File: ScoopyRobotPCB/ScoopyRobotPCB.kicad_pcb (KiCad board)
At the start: 2 copper layers, 25 parts, among them J1 18V battery, J2 Raspberry_Pi_Header, J3 Power, J4 Wheels, J5 Power, J6 Loading, J7 Left, J8 Right, M3 Left motor, M4 Right motor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

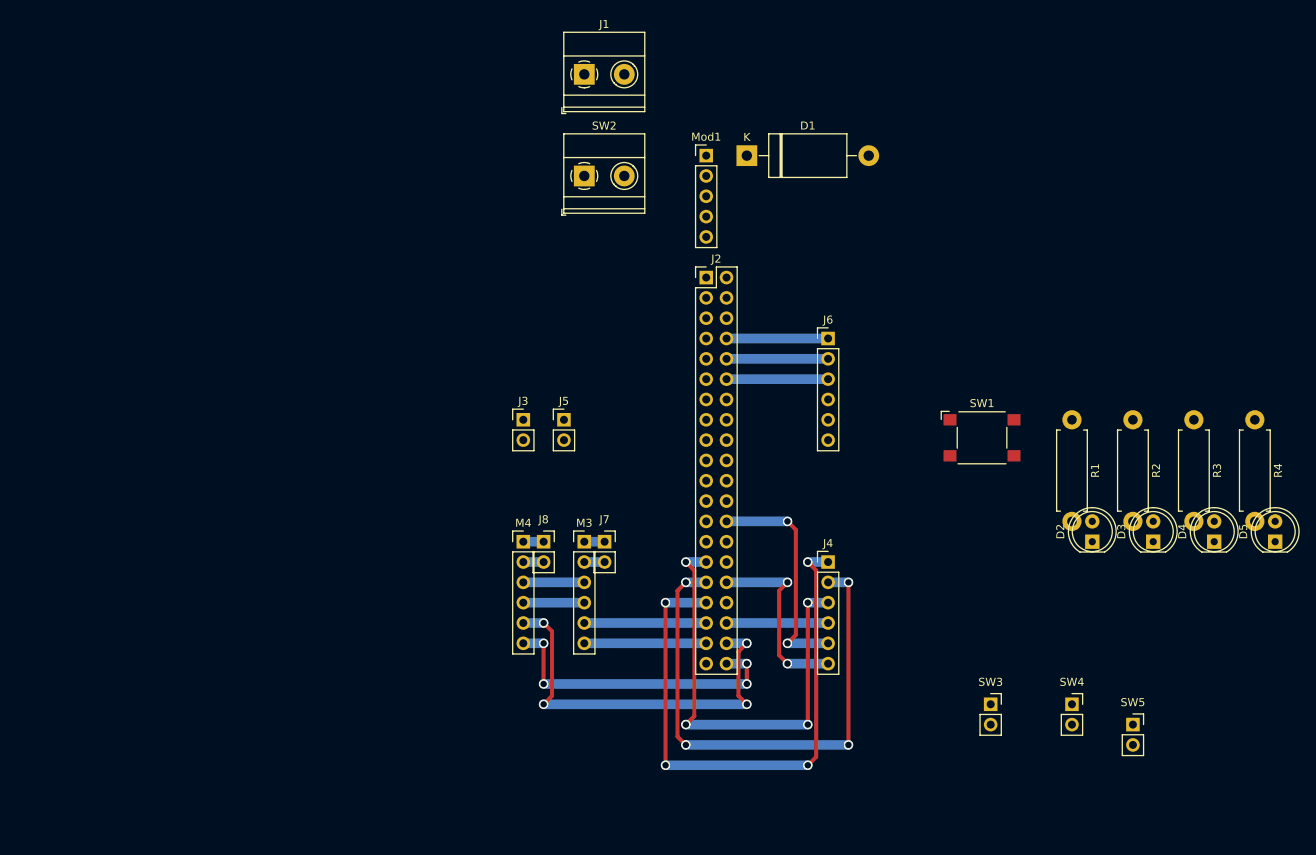
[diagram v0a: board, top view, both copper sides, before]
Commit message: Added voltage dividers for encoder, need to update layout to make way for ethernet header
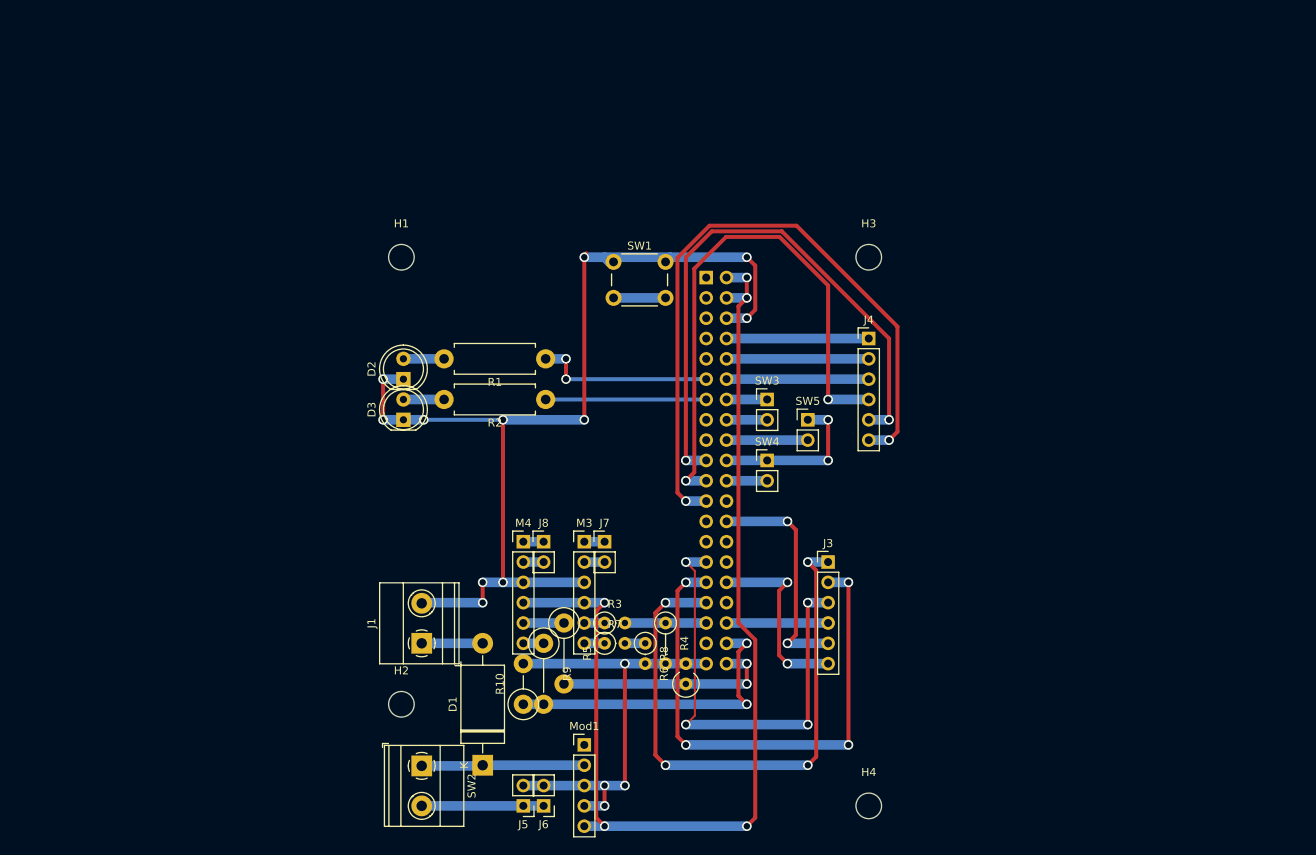
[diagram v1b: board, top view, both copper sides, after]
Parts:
- removed D4, D5: LED, LED_THT:LED_D5.0mm
- added H1: MountingHole, MountingHole:MountingHole_3.2mm_M3, F.Cu at (88.9, 76.2)
- added H2: MountingHole, MountingHole:MountingHole_3.2mm_M3, F.Cu at (88.9, 132.1)
- added H3: MountingHole, MountingHole:MountingHole_3.2mm_M3, F.Cu at (147.3, 76.2)
- added H4: MountingHole, MountingHole:MountingHole_3.2mm_M3, F.Cu at (147.3, 144.8)
- added R10: 2.2k, Resistor_THT:R_Axial_DIN0411_L9.9mm_D3.6mm_P5.08mm_Vertical, F.Cu at (104.1, 132.1)
- added R5: 1.5k, Resistor_THT:R_Axial_DIN0411_L9.9mm_D3.6mm_P7.62mm_Vertical, F.Cu at (109.2, 121.9)
- added R6: 2.2k, Resistor_THT:R_Axial_DIN0309_L9.0mm_D3.2mm_P2.54mm_Vertical, F.Cu at (124.5, 129.5)
- added R7: 1.5k, Resistor_THT:R_Axial_DIN0207_L6.3mm_D2.5mm_P2.54mm_Vertical, F.Cu at (114.3, 124.5)
- added R8: 2.2k, Resistor_THT:R_Axial_DIN0207_L6.3mm_D2.5mm_P2.54mm_Vertical, F.Cu at (119.4, 124.5)
- added R9: 1.5k, Resistor_THT:R_Axial_DIN0411_L9.9mm_D3.6mm_P7.62mm_Vertical, F.Cu at (106.7, 124.5)
- J2: footprint Connector_PinHeader_2.54mm:PinHeader_2x20_P2.54mm_Vertical -> Connector_PinSocket_2.54mm:PinSocket_2x20_P2.54mm_Vertical; moved to B.Cu
- J7, J8, SW3, SW4, SW5: footprint Connector_PinSocket_2.54mm:PinSocket_1x02_P2.54mm_Vertical -> Connector_PinHeader_2.54mm:PinHeader_1x02_P2.54mm_Vertical
- R3: value 220 -> 1.5k; footprint Resistor_THT:R_Axial_DIN0411_L9.9mm_D3.6mm_P12.70mm_Horizontal -> Resistor_THT:R_Axial_DIN0207_L6.3mm_D2.5mm_P2.54mm_Vertical
- R4: value 220 -> 2.2k; footprint Resistor_THT:R_Axial_DIN0411_L9.9mm_D3.6mm_P12.70mm_Horizontal -> Resistor_THT:R_Axial_DIN0207_L6.3mm_D2.5mm_P5.08mm_Vertical
- SW1: footprint Button_Switch_SMD:SW_SPST_Omron_B3FS-100xP -> Button_Switch_THT:SW_PUSH_6mm
- moved D3 95.0 mm to (89.2, 96.5)
- moved D2 88.5 mm to (89.2, 91.4)
- moved D1 83.0 mm to (99.1, 139.7), turned to 90 degrees
- moved R3 77.9 mm to (114.3, 121.9), turned to 0 degrees
- moved R4 77.9 mm to (121.9, 121.9)
- moved SW2 76.5 mm to (91.4, 139.8), turned to -90 degrees
- moved Mod1 75.2 mm to (111.8, 137.2)
- moved J1 74.0 mm to (91.4, 124.5), turned to 90 degrees
- moved R2 73.4 mm to (106.9, 94.0), turned to 180 degrees
- moved R1 66.2 mm to (106.9, 88.9), turned to 180 degrees
- moved SW5 55.7 mm to (139.7, 96.5)
- moved SW1 51.0 mm to (115.4, 76.8)
- moved SW4 48.8 mm to (134.6, 101.6)
- moved J6 48.3 mm to (106.7, 144.8), turned to 180 degrees
- moved J5 48.3 mm to (104.1, 144.8), turned to 180 degrees
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- renumbered J4 to J3, J6 to J4, J3 to J5, J5 to J6
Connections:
- J2 pad 11: /UI.LED2 -> /UI.LED0
- J2 pad 13: /UI.LED3 -> /UI.LED1
- J2 pad 3: /UI.SW -> unconnected-(J2-GPIO02/SDA-Pad3)
- J2 pad 5: /UI.LED0 -> unconnected-(J2-GPIO03/SCL-Pad5)
- J2 pad 7: /UI.LED1 -> /UI.SW
- M3 pad 5: /L.Enc_A -> Net-(M3-Enc_A)
- M3 pad 6: /L.Enc_B -> Net-(M3-Enc_B)
- M4 pad 5: /R.Enc_A -> Net-(M4-Enc_A)
- M4 pad 6: /R.Enc_B -> Net-(M4-Enc_B)
- R3 pad 1: /UI.LED2 -> Net-(M3-Enc_A)
- R3 pad 2: Net-(D4-A) -> /L.Enc_A
- R4 pad 1: /UI.LED3 -> /L.Enc_A
- R4 pad 2: Net-(D5-A) -> GND
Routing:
- net GND: track 7.62 -> 212.0 mm, vias 0 -> 17
- net +5V: track 7.62 -> 134.7 mm, vias 0 -> 5
- net /Tray.En: track 0.00 -> 84.9 mm, vias 0 -> 2
- net /Tray.Mot_A: track 0.00 -> 72.9 mm, vias 0 -> 2
- net /Tray.Mot_B: track 0.00 -> 69.7 mm, vias 0 -> 2
- net /UI.LED0: track 0.00 -> 22.6 mm, vias 0 -> 2
- net +BATT: track 0.00 -> 20.4 mm
- net /UI.LED1: track 0.00 -> 20.1 mm
- net Vdrive: track 0.00 -> 15.2 mm
- net /L.Enc_B: track 15.2 -> 2.54 mm
- net /R.Enc_A: track 50.0 -> 39.0 mm, vias 4 -> 2
- net /Tray up: track 0.00 -> 10.2 mm
- net /R.Enc_B: track 38.1 -> 27.9 mm, vias 4 -> 2
- net Net-(D1-A): track 0.00 -> 7.62 mm
- net /UI.SW: track 0.00 -> 6.50 mm
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
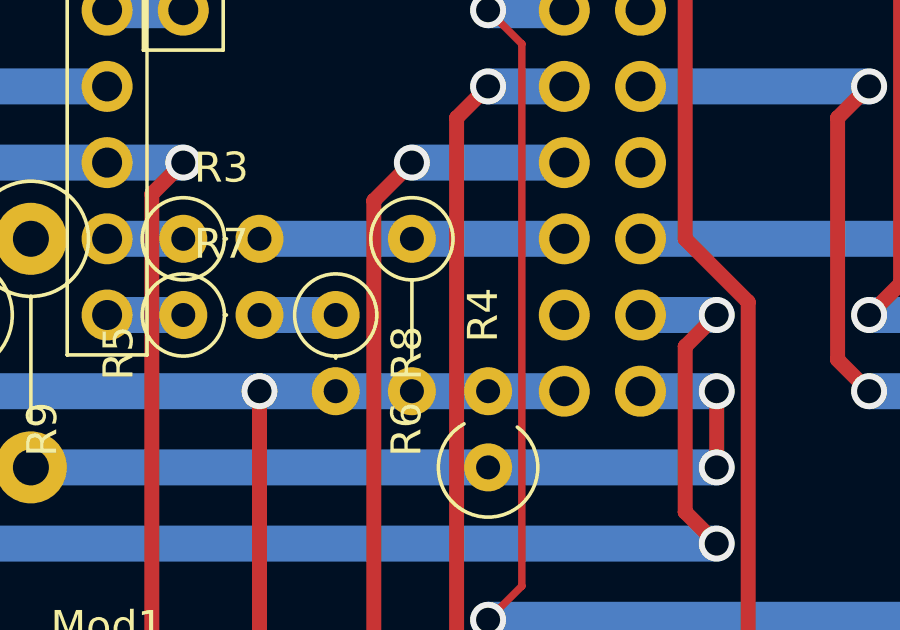
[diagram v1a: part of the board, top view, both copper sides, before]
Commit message: Added missing track on PCB
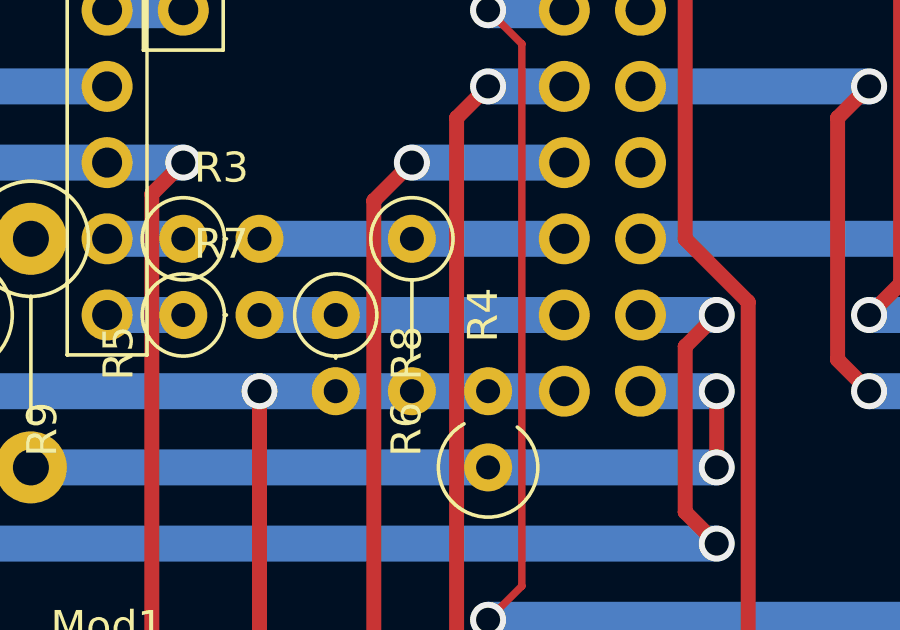
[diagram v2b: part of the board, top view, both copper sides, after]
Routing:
- net /L.Enc_B: track 2.54 -> 10.2 mm
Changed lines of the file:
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@@
+	)
+	(segment
+		(start 119.38 124.46)
+		(end 127 124.46)
+		(width 1.2)
+		(layer "B.Cu")
+		(net 17)
 	)
 	(segment

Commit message: Schematic finished
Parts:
- removed the J6 at (106.7, 144.8)
- removed SW4: Tray down, Connector_PinHeader_2.54mm:PinHeader_1x02_P2.54mm_Vertical
- removed SW5: Tray up, Connector_PinHeader_2.54mm:PinHeader_1x02_P2.54mm_Vertical
- added D4: 1N4004, Diode_THT:D_DO-41_SOD81_P10.16mm_Horizontal, F.Cu at (144.8, 86.4)
- added J3: Left colour sensor, Connector_PinHeader_2.54mm:PinHeader_1x04_P2.54mm_Vertical, F.Cu at (121.9, 86.4)
- added Q1: Q_NPN_Darlington_BCE, Package_TO_SOT_THT:TO-220-3_Vertical, F.Cu at (114.3, 59.4)
- added R3: 390, Resistor_THT:R_Axial_DIN0411_L9.9mm_D3.6mm_P7.62mm_Vertical, F.Cu at (113.6, 52.9)
- J4: value Loading -> Right colour sensor; footprint Connector_PinHeader_2.54mm:PinHeader_1x06_P2.54mm_Vertical -> Connector_PinHeader_2.54mm:PinHeader_1x04_P2.54mm_Vertical
- R10: renamed from R9; value 1.5k -> 10k
- R11: renamed from R10; value 2.2k -> 10k
- R4: renamed from R3; value 1.5k -> 10k; footprint Resistor_THT:R_Axial_DIN0207_L6.3mm_D2.5mm_P2.54mm_Vertical -> Resistor_THT:R_Axial_DIN0411_L9.9mm_D3.6mm_P7.62mm_Vertical
- R5: renamed from R4; value 2.2k -> 10k; footprint Resistor_THT:R_Axial_DIN0207_L6.3mm_D2.5mm_P5.08mm_Vertical -> Resistor_THT:R_Axial_DIN0207_L6.3mm_D2.5mm_P2.54mm_Vertical
- R6: renamed from R5; value 1.5k -> 10k
- R7: renamed from R6; value 2.2k -> 10k
- R8: renamed from R7; value 1.5k -> 10k; footprint Resistor_THT:R_Axial_DIN0207_L6.3mm_D2.5mm_P2.54mm_Vertical -> Resistor_THT:R_Axial_DIN0411_L9.9mm_D3.6mm_P7.62mm_Vertical
- R9: renamed from R8; value 2.2k -> 10k; footprint Resistor_THT:R_Axial_DIN0207_L6.3mm_D2.5mm_P2.54mm_Vertical -> Resistor_THT:R_Axial_DIN0411_L9.9mm_D3.6mm_P5.08mm_Vertical
- moved H1 43.4 mm to (45.5, 76.2)
- moved D2 43.4 mm to (45.7, 91.4)
- moved D3 43.4 mm to (45.7, 96.5)
- moved R1 43.4 mm to (63.5, 88.9)
- moved R2 43.4 mm to (63.5, 94.0)
- moved SW1 43.4 mm to (72.0, 76.8)
- moved J4 14.4 mm to (137.2, 96.5)
- moved SW3 8.03 mm to (132.1, 101.6)
- renumbered J3 to J5, J5 to J6, M3 to M2, M4 to M3
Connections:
- J2 pad 10: /Roll.Mot_A -> /Chain motor
- J2 pad 12: /Roll.Mot_B -> unconnected-(J2-PWM0/GPIO18-Pad12)
- J2 pad 16: /Roll position -> /RC.SDA
- J2 pad 18: /Tray up -> /RC.SCL
- J2 pad 19: /Tray.Mot_A -> unconnected-(J2-GPIO10/MOSI0-Pad19)
- J2 pad 21: /Tray.Mot_B -> unconnected-(J2-GPIO09/MISO0-Pad21)
- J2 pad 22: /Tray down -> /Chain position
- J2 pad 23: /Tray.En -> unconnected-(J2-GPIO11/SCLK0-Pad23)
- J2 pad 29: /L.Mot_A -> unconnected-(J2-GPIO05/GCLK1-Pad29)
- J2 pad 3: unconnected-(J2-GPIO02/SDA-Pad3) -> /LC.SCL
- J2 pad 5: unconnected-(J2-GPIO03/SCL-Pad5) -> /LC.SDA
- J2 pad 8: /Roll.En -> unconnected-(J2-TXD/GPIO14-Pad8)
- J4 pad 1: /Roll.En -> /RC.SDA
- J4 pad 2: /Roll.Mot_A -> /RC.SCL
- J4 pad 3: /Roll.Mot_B -> GND
- J4 pad 4: /Tray.Mot_B -> +3.3V
- SW3 pad 2: /Roll position -> /Chain position
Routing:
- net /Tray.En: track 84.9 -> 0.00 mm, vias 2 -> 0
- net /Tray.Mot_A: track 72.9 -> 0.00 mm, vias 2 -> 0
- net /Tray.Mot_B: track 69.7 -> 0.00 mm, vias 2 -> 0
- net +3.3V: track 0.00 -> 51.3 mm, vias 0 -> 1
- net /Roll.Mot_B: track 17.8 -> 0.00 mm
- net /Roll.Mot_A: track 17.8 -> 0.00 mm
- net /Roll.En: track 17.8 -> 0.00 mm
- net /Tray up: track 10.2 -> 0.00 mm
- net /RC.SDA: track 0.00 -> 7.62 mm
- net /RC.SCL: track 0.00 -> 7.62 mm
- net GND: track 212.0 -> 204.9 mm
- net /LC.SDA: track 0.00 -> 6.13 mm
- net /LC.SCL: track 0.00 -> 6.13 mm
- net /Tray down: track 5.08 -> 0.00 mm
- net /Roll position: track 5.08 -> 0.00 mm
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
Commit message: PCB layout updated to currentish
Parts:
- added M1: Chain gearmotor, Connector_PinHeader_2.54mm:PinHeader_1x02_P2.54mm_Vertical, F.Cu at (147.3, 88.9)
- D4: footprint Diode_THT:D_DO-41_SOD81_P10.16mm_Horizontal -> Diode_THT:D_DO-41_SOD81_P2.54mm_Vertical_KathodeUp
- R3: footprint Resistor_THT:R_Axial_DIN0411_L9.9mm_D3.6mm_P7.62mm_Vertical -> Resistor_THT:R_Axial_DIN0411_L9.9mm_D3.6mm_P5.08mm_Vertical
- moved R3 40.4 mm to (132.1, 88.9)
- moved Q1 38.9 mm to (139.7, 88.9), turned to 90 degrees
- moved D4 2.54 mm to (144.8, 88.9), turned to 90 degrees
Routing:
- net Vdrive: track 15.2 -> 114.7 mm
- net Net-(D4-A): track 0.00 -> 7.62 mm
- net GND: track 204.9 -> 212.6 mm
- net +3.3V: track 51.3 -> 54.9 mm
- net /Chain motor: track 0.00 -> 2.54 mm
- net Net-(Q1-B): track 0.00 -> 2.54 mm
